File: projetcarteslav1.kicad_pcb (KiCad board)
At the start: 2 copper layers, 95 parts, among them K1 Galvo X, K2 Galvo Y, K3 Galvo pwr, P1 I2C, P10 SW_AMIN, P11 SW_AMAX, P12 ROT_ENC, P13 FAN, P14 Laser pwr, P2 SCREEN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

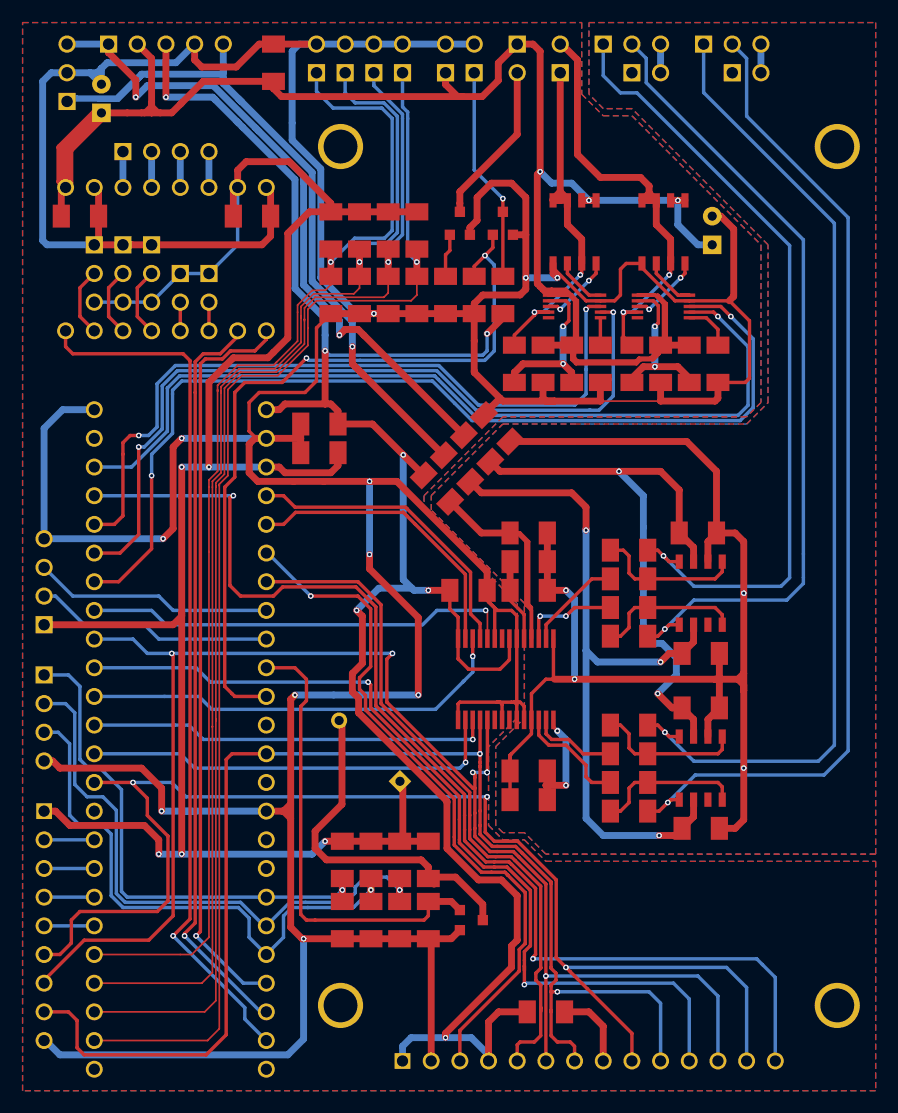
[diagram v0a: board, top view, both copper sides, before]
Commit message: Fixed C5 silkscreen, fixed shorts of speaker terminals.
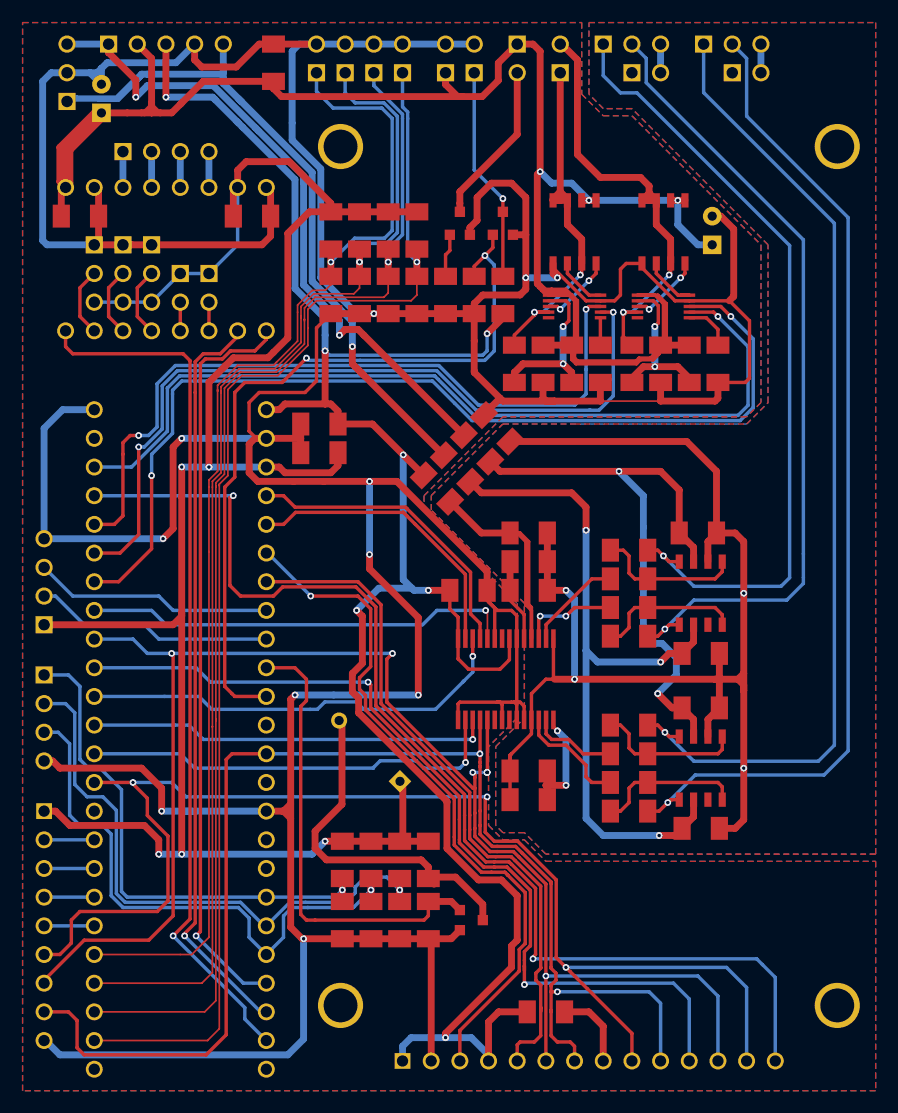
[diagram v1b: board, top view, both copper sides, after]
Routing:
- net /I2S_MCLK: track 37.4 -> 38.0 mm
- net /I2S_BCLK: track 38.5 -> 39.1 mm
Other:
- net class Default: via_dia 0.508 -> 0.6; via_drill 0.254 -> 0.3
- rule trace_min: 0.3 -> 0.15
- rule via_min_drill: 0.254 -> 0.3
- rule via_min_size: 0.508 -> 0.6
